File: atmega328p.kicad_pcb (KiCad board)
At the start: 2 copper layers, 68.6 x 53.3 mm, 40 parts, among them CON1 Micro USB, CON2 AVR-ISP-6, IC1 DS3231M, IC2 LD1117, IC3 ATMEGA328-P, M1 D1, P5 CONN_1, P6 CONN_1, P7 CONN_1, P8 CONN_1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

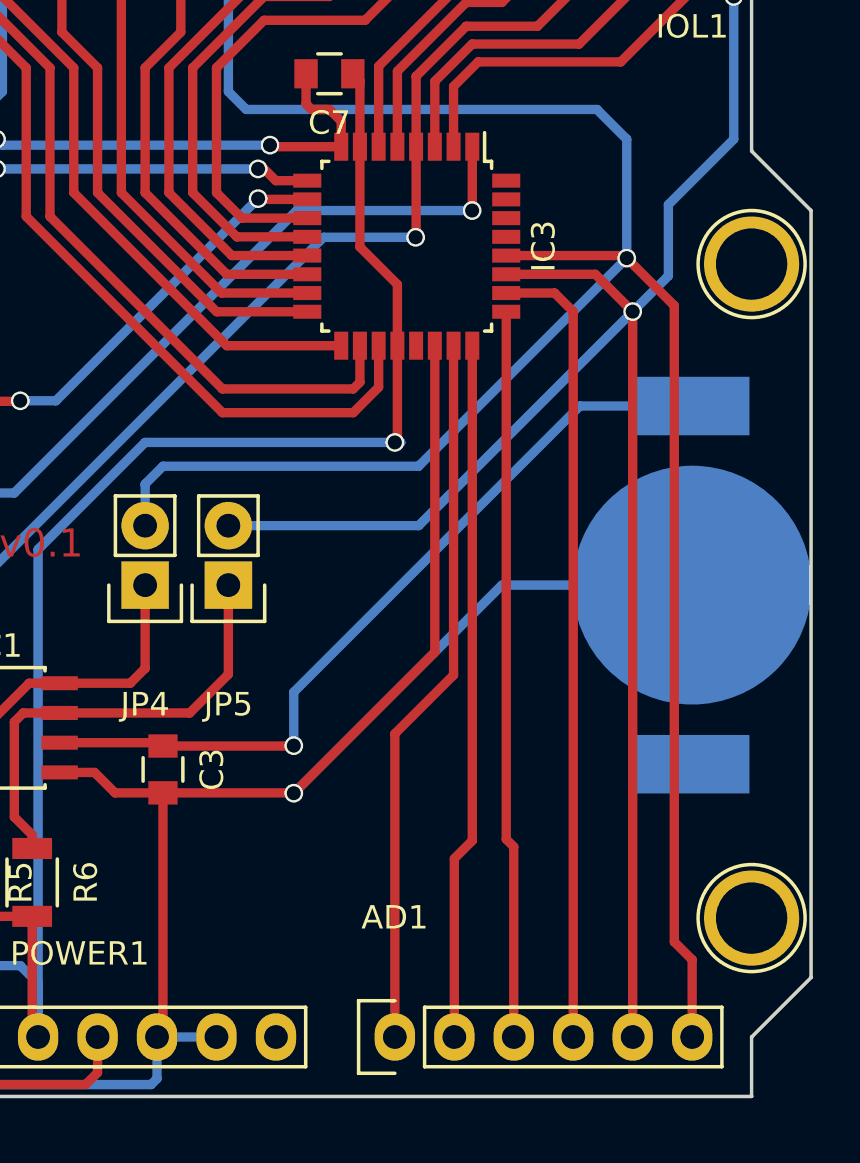
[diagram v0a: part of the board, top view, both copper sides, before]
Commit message: change batt holder due to wrong footprint
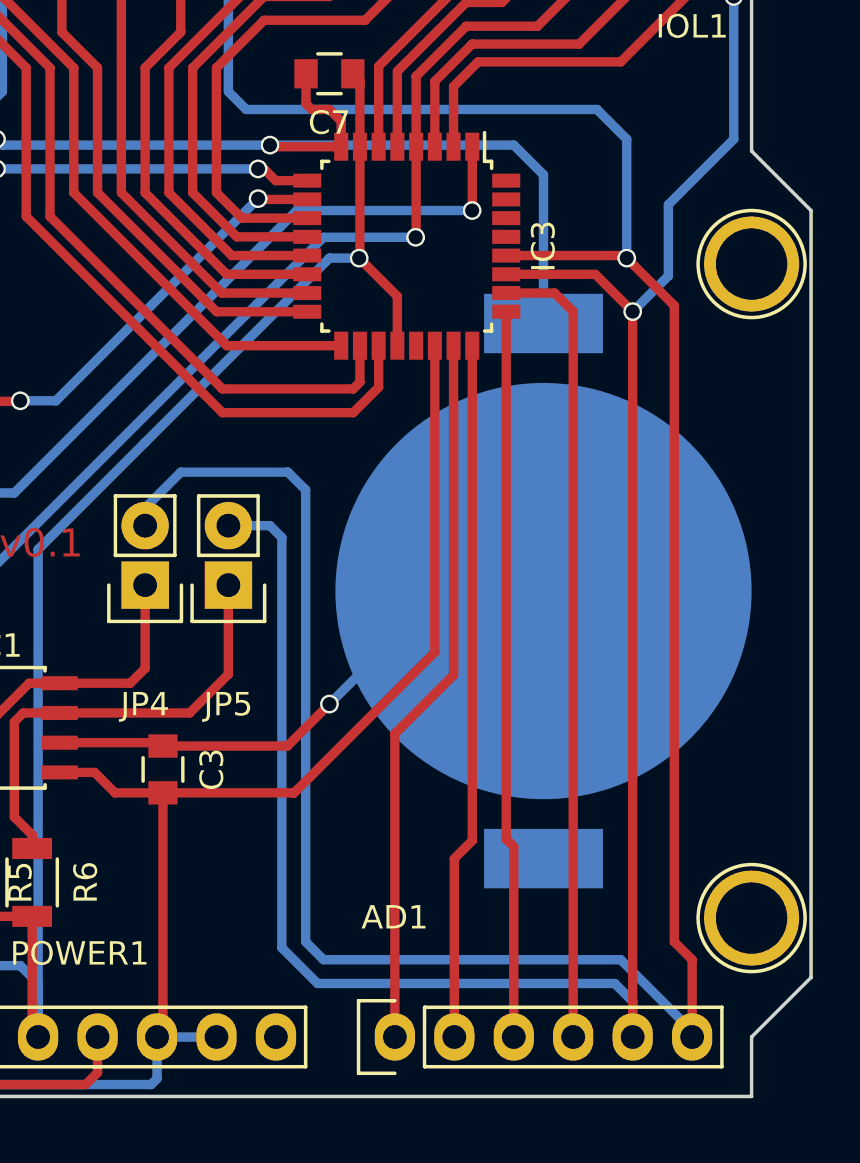
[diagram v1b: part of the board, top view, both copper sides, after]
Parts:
- BATT1: footprint open-project:BAT_CR1216 -> .pretty:20mmBattHolder
- moved BATT1 6.36 mm to (168.1, 104.8)
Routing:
- net SCL: track 124.8 -> 144.7 mm
- net SDA: track 123.8 -> 140.2 mm
- net Net-(BATT1-Pad1): track 36.7 -> 23.5 mm
- net +3V3: track 139.4 -> 136.4 mm
- net GND: track 300.2 -> 298.1 mm, vias 5 -> 4
